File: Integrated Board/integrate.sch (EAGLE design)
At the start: 67 parts, among them U1 LM293D-SOIC8, U2 LM293D-SOIC8, U3 LM293D-SOIC8, U4 LM293D-SOIC8, U5 LM293D-SOIC8, U6 LM293D-SOIC8, U7 LM293D-SOIC8, U8 LM293D-SOIC8

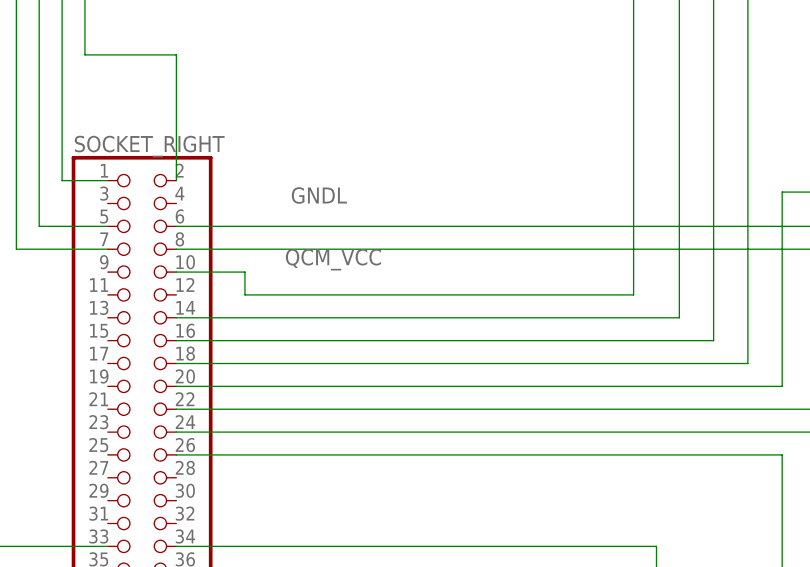
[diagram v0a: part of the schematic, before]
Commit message: Revert "20180712-change-pin"
This reverts commit fb38f18733497d936434fddb3c409504ab7d6048.
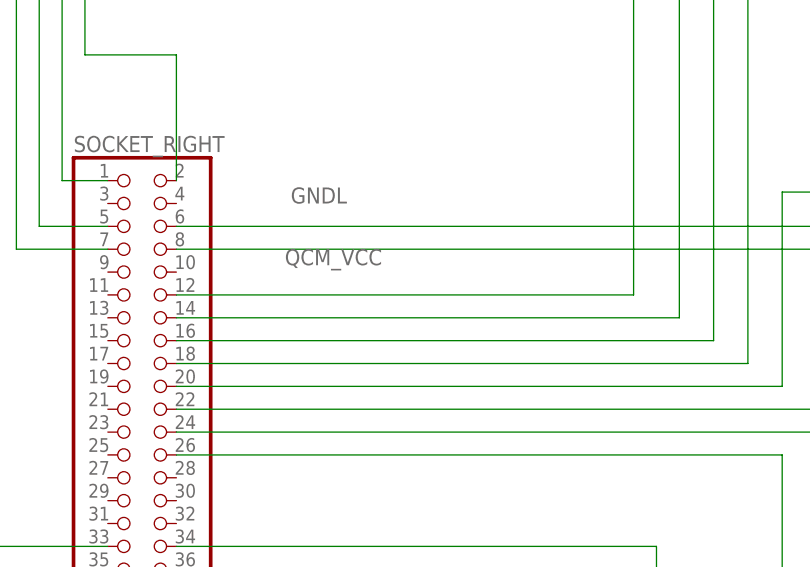
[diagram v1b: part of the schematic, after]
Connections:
- net S1: now also SOCKET_RIGHT.12; no longer SOCKET_RIGHT.10
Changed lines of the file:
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@@
 <setting verticaltext="up"/>
 </settings>
-<grid distance="0.1" unitdist="inch" unit="inch" style="lines" multiple="1" display="no" altdistance="0.01" altunitdist="inch" altunit="inch"/>
+<grid distance="30" unitdist="mil" unit="mil" style="lines" multiple="1" display="yes" altdistance="30" altunitdist="mil" altunit="mil"/>
 <layers>
 <layer number="1" name="Top" color="4" fill="1" visible="no" active="no"/>
@@
 <wire x1="335.28" y1="184.15" x2="271.78" y2="184.15" width="0.1524" layer="91"/>
 <wire x1="271.78" y1="184.15" x2="271.78" y2="76.2" width="0.1524" layer="91"/>
+<pinref part="SOCKET_RIGHT" gate="A" pin="12"/>
+<wire x1="271.78" y1="76.2" x2="220.98" y2="76.2" width="0.1524" layer="91"/>
 <label x="332.74" y="187.96" size="1.778" layer="95"/>
-<wire x1="271.78" y1="76.2" x2="228.6" y2="76.2" width="0.1524" layer="91"/>
-<wire x1="228.6" y1="76.2" x2="228.6" y2="78.74" width="0.1524" layer="91"/>
-<pinref part="SOCKET_RIGHT" gate="A" pin="10"/>
-<wire x1="228.6" y1="78.74" x2="220.98" y2="78.74" width="0.1524" layer="91"/>
-</segment>
-</net>
+</segment>
+</net>

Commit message: 20180719-Fix-problem-for-LVB
1. OSC part: left top 6th channel cannot be arranged, change pin to left top 5th

2.change the area of HVB
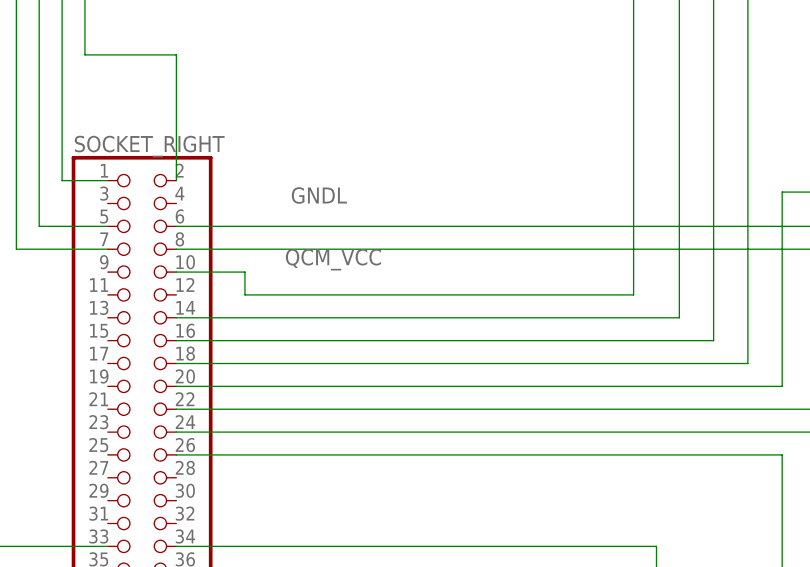
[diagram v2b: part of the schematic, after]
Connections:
- net S1: now also SOCKET_RIGHT.10; no longer SOCKET_RIGHT.12
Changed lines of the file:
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@@
 <setting verticaltext="up"/>
 </settings>
-<grid distance="30" unitdist="mil" unit="mil" style="lines" multiple="1" display="yes" altdistance="30" altunitdist="mil" altunit="mil"/>
+<grid distance="0.1" unitdist="inch" unit="inch" style="lines" multiple="1" display="no" altdistance="0.01" altunitdist="inch" altunit="inch"/>
 <layers>
 <layer number="1" name="Top" color="4" fill="1" visible="no" active="no"/>
@@
 <wire x1="335.28" y1="184.15" x2="271.78" y2="184.15" width="0.1524" layer="91"/>
 <wire x1="271.78" y1="184.15" x2="271.78" y2="76.2" width="0.1524" layer="91"/>
-<pinref part="SOCKET_RIGHT" gate="A" pin="12"/>
-<wire x1="271.78" y1="76.2" x2="220.98" y2="76.2" width="0.1524" layer="91"/>
 <label x="332.74" y="187.96" size="1.778" layer="95"/>
-</segment>
-</net>
+<wire x1="271.78" y1="76.2" x2="228.6" y2="76.2" width="0.1524" layer="91"/>
+<wire x1="228.6" y1="76.2" x2="228.6" y2="78.74" width="0.1524" layer="91"/>
+<pinref part="SOCKET_RIGHT" gate="A" pin="10"/>
+<wire x1="228.6" y1="78.74" x2="220.98" y2="78.74" width="0.1524" layer="91"/>
+</segment>
+</net>
